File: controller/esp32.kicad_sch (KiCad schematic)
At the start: 24 parts, among them J2 Debug, J3 Conn_01x06, J6 Jumper, Q1 MMBT3904, Q2 MMBT3904, SW1 SW_SPST, SW2 SW_SPST, U3 NRF24L01_Breakout, U4 ADS7828, U5 ESP32-WROOM-32U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

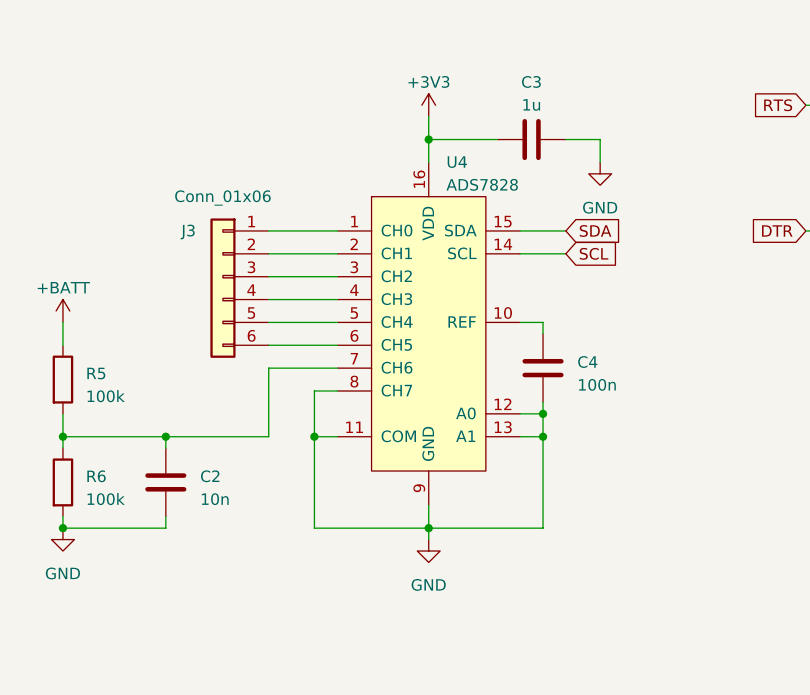
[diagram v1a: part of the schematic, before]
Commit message: Put ADC Vref onto analog connector.
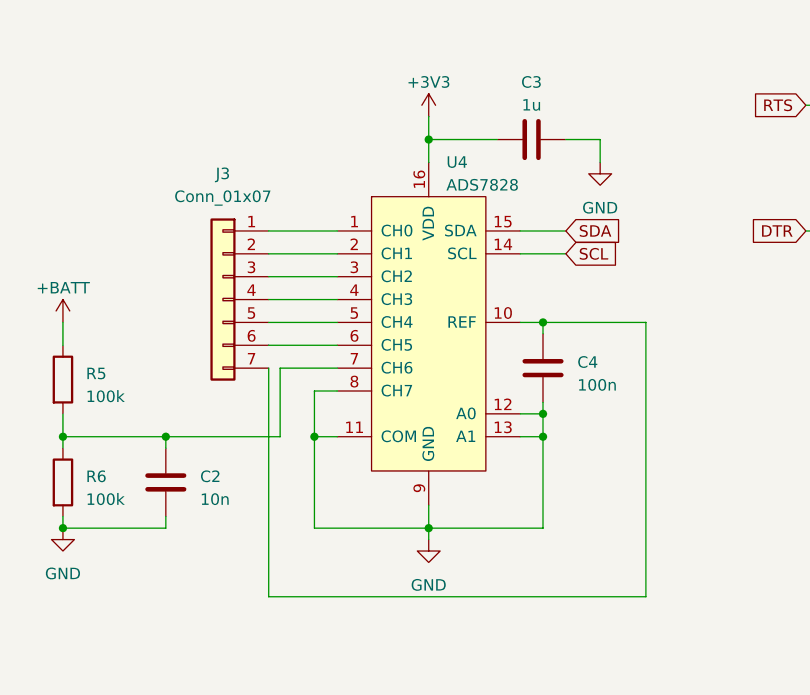
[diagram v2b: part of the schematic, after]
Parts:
- removed J3: Conn_01x06, Connector_JST:JST_XH_B06B-XH-A_1x06_P2.50mm_Vertical, symbol Connector_Generic:Conn_01x06
- added J3: Conn_01x07, Connector_JST:JST_XH_B07B-XH-A_1x07_P2.50mm_Vertical, symbol Connector_Generic:Conn_01x07
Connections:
- net at C4.1, U4.10 (REF): now also J3.7 (Pin_7)
- net at U4.1 (CH0): now also J3.1 (Pin_1)
- net at U4.2 (CH1): now also J3.2 (Pin_2)
- net at U4.3 (CH2): now also J3.3 (Pin_3)
- net at U4.4 (CH3): now also J3.4 (Pin_4)
- net at U4.5 (CH4): now also J3.5 (Pin_5)
- net at U4.6 (CH5): now also J3.6 (Pin_6)
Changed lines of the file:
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@@
 	)
 	(junction
+		(at 173.99 129.54)
+		(diameter 0)
+		(color 0 0 0 0)
+	)
+	(junction
 		(at 233.68 111.76)
 		(diameter 0)
@@
 	(wire
 		(pts
-			(xy 151.13 134.62) (xy 143.51 134.62)
-		)
-		(stroke
-			(width 0)
-			(type default)
-		)
-	)
-	(wire
-		(pts
 			(xy 173.99 138.43) (xy 173.99 139.7)
 		)
@@
 	(wire
 		(pts
+			(xy 143.51 160.02) (xy 185.42 160.02)
+		)
+		(stroke
+			(width 0)
+			(type default)
+		)
+	)
+	(wire
+		(pts
 			(xy 182.88 67.31) (xy 182.88 68.58)
 		)
@@
 	(wire
 		(pts
+			(xy 143.51 134.62) (xy 143.51 160.02)
+		)
+		(stroke
+			(width 0)
+			(type default)
+		)
+	)
+	(wire
+		(pts
 			(xy 228.6 76.2) (xy 228.6 77.47)
 		)
@@
 	(wire
 		(pts
-			(xy 143.51 142.24) (xy 132.08 142.24)
+			(xy 132.08 142.24) (xy 144.78 142.24)
 		)
 		(stroke
@@
 	(wire
 		(pts
+			(xy 144.78 134.62) (xy 144.78 142.24)
+		)
+		(stroke
+			(width 0)
+			(type default)
+		)
+	)
+	(wire
+		(pts
 			(xy 171.45 142.24) (xy 173.99 142.24)
 		)
@@
 	(wire
 		(pts
+			(xy 185.42 160.02) (xy 185.42 129.54)
+		)
+		(stroke
+			(width 0)
+			(type default)
+		)
+	)
+	(wire
+		(pts
 			(xy 233.68 142.24) (xy 233.68 144.78)
 		)
@@
 	(wire
 		(pts
+			(xy 151.13 134.62) (xy 144.78 134.62)
+		)
+		(stroke
+			(width 0)
+			(type default)
+		)
+	)
+	(wire
+		(pts
 			(xy 228.6 50.8) (xy 228.6 55.88)
 		)
@@
 	(wire
 		(pts
-			(xy 143.51 134.62) (xy 143.51 142.24)
+			(xy 185.42 129.54) (xy 173.99 129.54)
 		)
 		(stroke
@@
 	)
 	(symbol
+		(lib_id "Connector_Generic:Conn_01x07")
+		(at 138.43 127 0)
+		(mirror y)
+		(unit 1)
+		(exclude_from_sim no)
+		(in_bom yes)
+		(on_board yes)
+		(dnp no)
+		(fields_autoplaced yes)
+		(property "Reference" "J3"
+			(at 138.43 113.03 0)
+			(effects
+				(font
+					(size 1.27 1.27)
+				)
+			)
+		)
+		(property "Value" "Conn_01x07"
+			(at 138.43 115.57 0)
+			(effects
+				(font
+					(size 1.27 1.27)
+				)
+			)
+		)
+		(property "Footprint" "Connector_JST:JST_XH_B07B-XH-A_1x07_P2.50mm_Vertical"
+			(at 138.43 127 0)
+			(effects
+				(font
+					(size 1.27 1.27)
+				)
+				(hide yes)
+			)
+		)
+		(property "Datasheet" "~"
+			(at 138.43 127 0)
+			(effects
+				(font
+					(size 1.27 1.27)
+				)
+				(hide yes)
+			)
+		)
+		(property "Description" "Generic connector, single row, 01x07, script generated (kicad-library-utils/schlib/autogen/connector/)"
+			(at 138.43 127 0)
+			(effects
+				(font
+					(size 1.27 1.27)
+				)
+				(hide yes)
+			)
+		)
+		(pin "5"
+		)
+		(pin "1"
+		)
+		(pin "4"
+		)
+		(pin "3"
+		)
+		(pin "2"
+		)
+		(pin "7"
+		)
+		(pin "6"
+		)
+		(instances
+			(project ""
+				(path "/0776e334-fbf5-4a46-a47e-c7e0521e2a6b/c55c2b6b-f055-464f-92b0-146d6ac0bfa3"
+					(reference "J3")
+					(unit 1)
+				)
+			)
+		)
+	)
+	(symbol
 		(lib_id "Connector_Generic:Conn_01x06")
 		(at 247.65 71.12 0)
@@
 					(unit 1)
 				)
-			)
-		)
-	)
-	(symbol
-		(lib_id "Connector_Generic:Conn_01x06")
-		(at 138.43 124.46 0)
-		(mirror y)
-		(unit 1)
-		(exclude_from_sim no)
-		(in_bom yes)
-		(on_board yes)
-		(dnp no)
-		(property "Reference" "J3"
-			(at 134.62 119.38 0)
-			(effects
-				(font
-					(size 1.27 1.27)
-				)
-			)
-		)
-		(property "Value" "Conn_01x06"
-			(at 138.43 115.57 0)
-			(effects
-				(font
-					(size 1.27 1.27)
-				)
-			)
-		)
-		(property "Footprint" "Connector_JST:JST_XH_B06B-XH-A_1x06_P2.50mm_Vertical"
-			(at 138.43 124.46 0)
-			(effects
-				(font
-					(size 1.27 1.27)
-				)
-				(hide yes)
-			)
-		)
-		(property "Datasheet" "~"
-			(at 138.43 124.46 0)
-			(effects
-				(font
-					(size 1.27 1.27)
-				)
-				(hide yes)
-			)
-		)
-		(property "Description" ""
-			(at 138.43 124.46 0)
-			(effects
-				(font
-					(size 1.27 1.27)
-				)
-				(hide yes)
-			)
-		)
-		(pin "1"
-		)
-		(pin "2"
-		)
-		(pin "3"
-		)
-		(pin "4"
-		)
-		(pin "5"
-		)
-		(pin "6"
-		)
-		(instances
-			(project "remote"
-				(path "/0776e334-fbf5-4a46-a47e-c7e0521e2a6b/c55c2b6b-f055-464f-92b0-146d6ac0bfa3"
-					(reference "J3")
-					(unit 1)
-				)

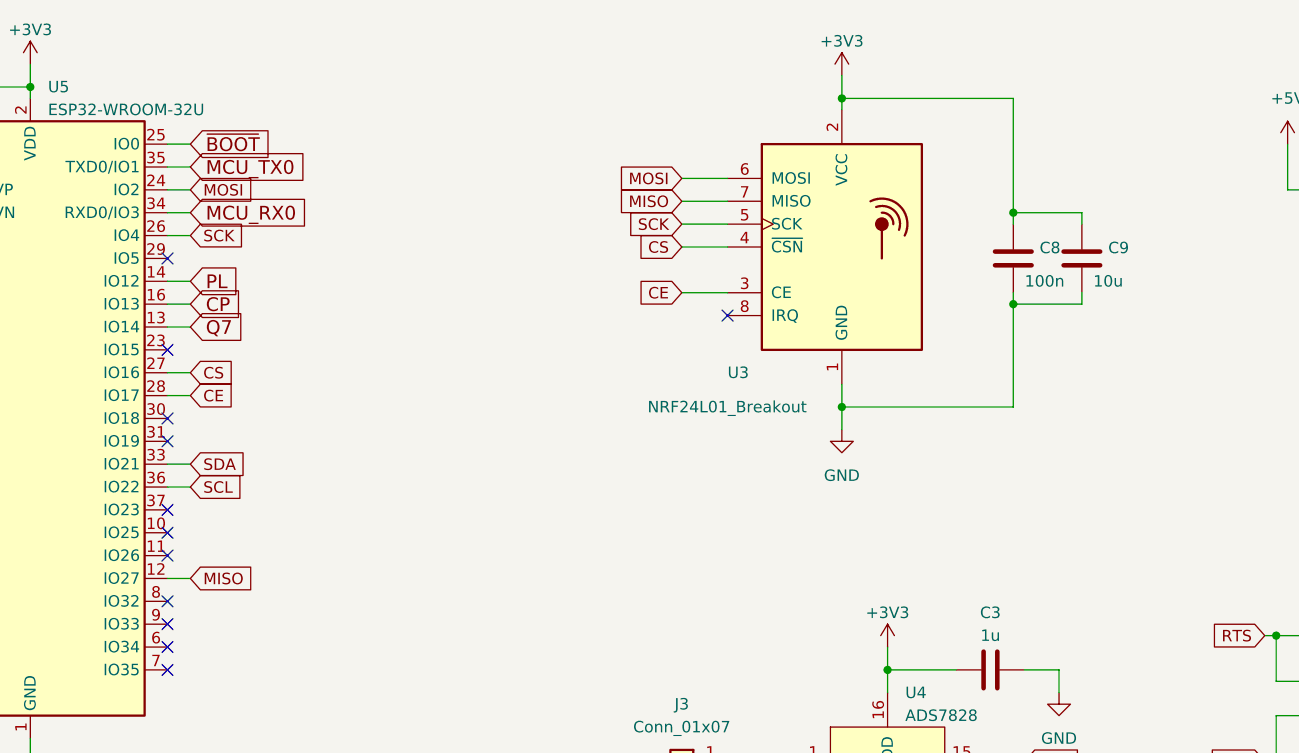
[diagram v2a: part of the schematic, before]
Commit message: Remove nRF24L01.
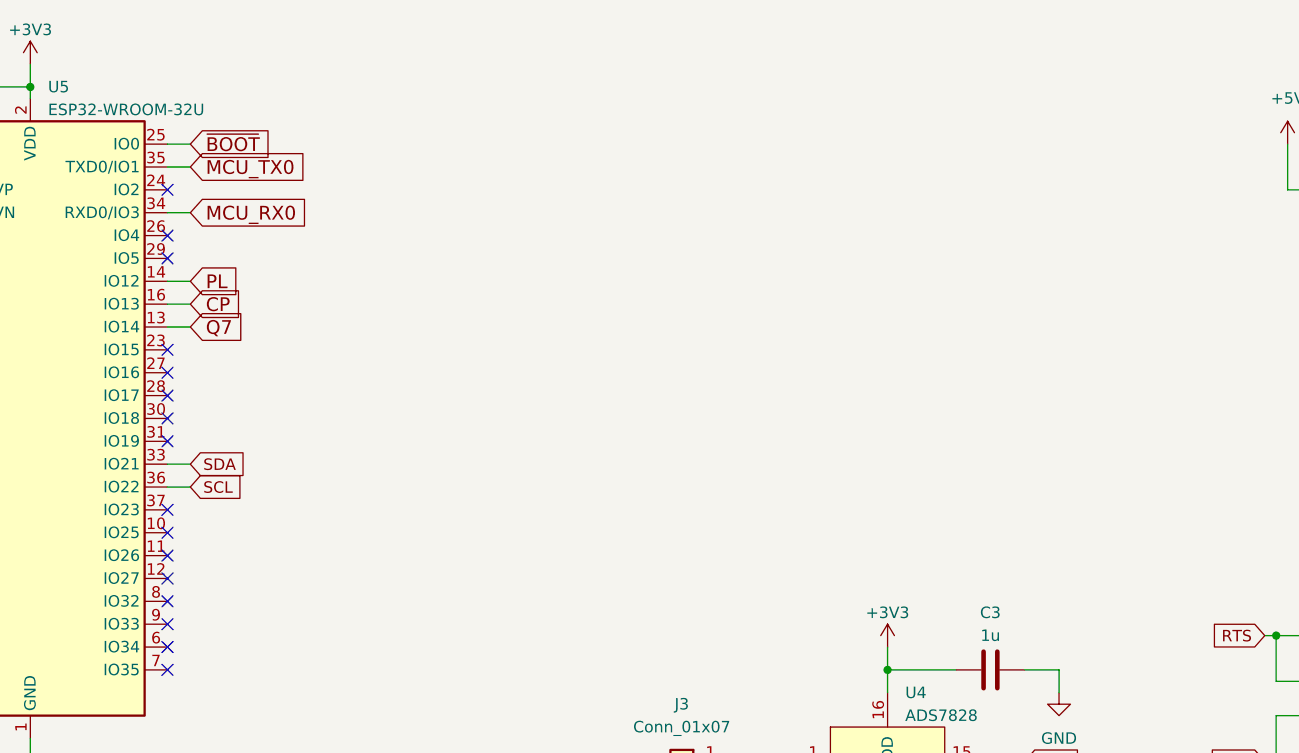
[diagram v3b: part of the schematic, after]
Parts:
- removed C8: 100n, Capacitor_SMD:C_0603_1608Metric, symbol Device:C
- removed C9: 10u, Capacitor_SMD:C_0603_1608Metric, symbol Device:C
- removed U3: NRF24L01_Breakout, RF_Module:nRF24L01_Breakout, symbol RF:NRF24L01_Breakout
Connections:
- net CE: no longer names the net of U5.28 (IO17)
- net CS: no longer names the net of U5.27 (IO16)
- net MISO: no longer names the net of U5.12 (IO27)
- net MOSI: no longer names the net of U5.24 (IO2)
- net SCK: no longer names the net of U5.26 (IO4)
- no-connect marks 20 -> 24

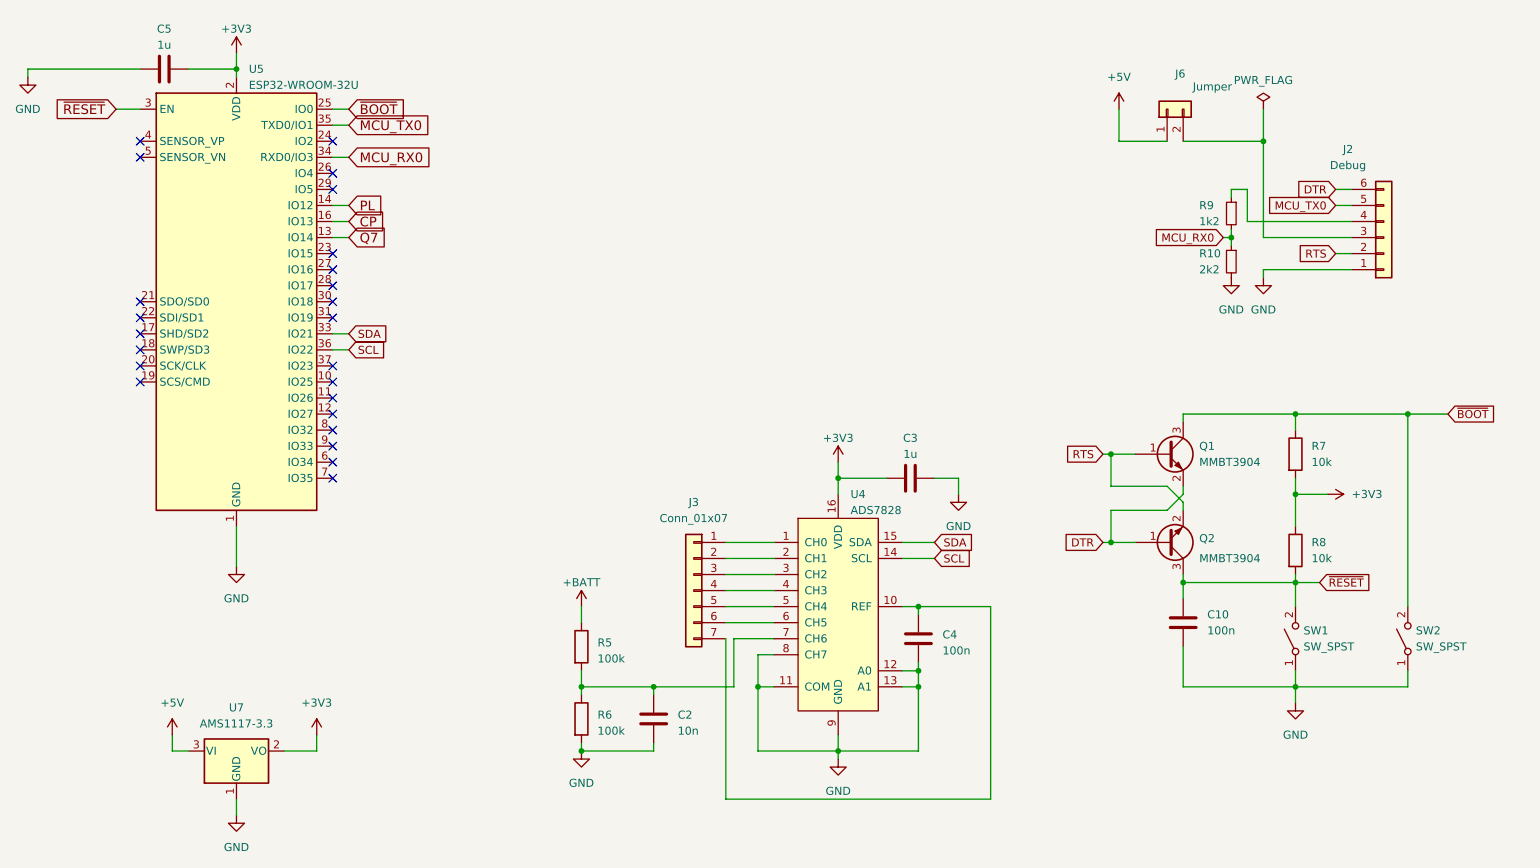
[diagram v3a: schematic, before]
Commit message: Power directly from battery.
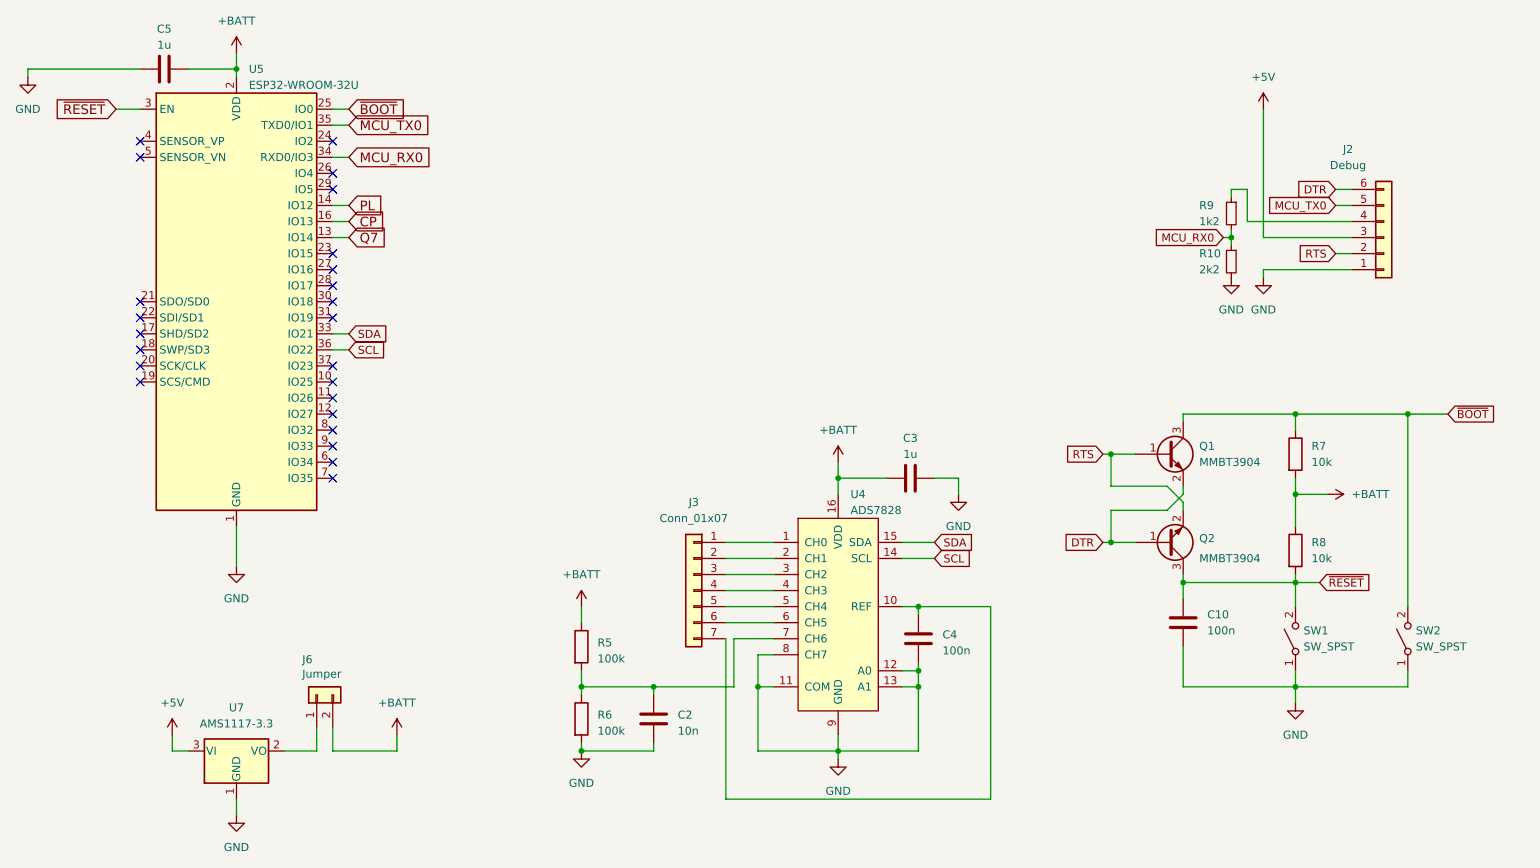
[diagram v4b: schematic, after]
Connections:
- net +5V: now also J2.3 (Pin_3); no longer J6.1 (Pin_1)
- net +BATT: now also C3.1, C5.2, J6.2 (Pin_2), R7.2, R8.1, U4.16 (VDD), U5.2 (VDD)
- removed net +3V3: C3.1, C5.2, R7.2, R8.1, U4.16 (VDD), U5.2 (VDD), U7.2 (VO)
- new net: J6.1 (Pin_1), U7.2 (VO)
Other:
- moved on the sheet: J6
